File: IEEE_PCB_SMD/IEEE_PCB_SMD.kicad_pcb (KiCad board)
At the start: 2 copper layers, 98.9 x 105.3 mm, 18 parts, among them U1 555, U2 4017, U3 EG1218, U4 1058TR

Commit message: SMD Rev3
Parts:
- added D10: D, IEEE_PCB_Ornament:SDM20U40Q, F.Cu at (153.6, 81.5)
- added D11: D, IEEE_PCB_Ornament:SDM20U40Q, F.Cu at (153.6, 84.2)
- added D12: D, IEEE_PCB_Ornament:SDM20U40Q, F.Cu at (153.6, 86.9)
- added G***: LOGO, Logos:IEEE Logo, F.Cu at (141.4, 100.6)
- added U5: CR2025TR, IEEE_PCB_Ornament:CR2025TR, F.Cu at (145.0, 95.8)
- RV1: value 500K -> 100K
- U4: value 1058TR -> EG1218; footprint IEEE_PCB_Ornament:1058TR -> IEEE_PCB_Ornament:EG1218
- moved D3 68.2 mm to (145.7, 128.7)
- moved D2 59.8 mm to (177.0, 74.9), turned to 90 degrees
- moved U4 20.3 mm to (152.2, 111.8), turned to 0 degrees
- moved RV1 19.5 mm to (145.0, 80.7)
- moved U3 13.1 mm to (138.5, 111.8)
- moved D8 10.9 mm to (144.9, 88.7), turned to 180 degrees
- moved C2 10.4 mm to (131.4, 93.4)
- moved D9 9.58 mm to (148.7, 94.5), turned to 0 degrees
- moved U2 9.21 mm to (157.3, 79.3)
- moved C1 8.84 mm to (125.0, 93.1)
- moved D7 7.04 mm to (141.2, 94.5)
- moved D6 6.50 mm to (176.2, 112.6), turned to 90 degrees
- moved D1 6.48 mm to (114.4, 74.7), turned to 270 degrees
- moved R1 6.45 mm to (138.7, 73.9)
- moved D4 6.29 mm to (144.8, 57.4)
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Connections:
- D1 pad 2: Net-(D1-Pad2) -> ALLON
- D2 pad 2: Net-(D1-Pad2) -> ALLON
- D3 pad 2: Net-(D1-Pad2) -> ALLON
- D4 pad 2: Net-(D4-Pad2) -> ALLON
- D5 pad 2: Net-(D4-Pad2) -> ALLON
- D6 pad 2: Net-(D4-Pad2) -> ALLON
- D7 pad 2: Net-(D7-Pad2) -> ALLON
- D8 pad 2: Net-(D7-Pad2) -> ALLON
- D9 pad 2: Net-(D7-Pad2) -> ALLON
- U2 pad 2: Net-(D1-Pad2) -> Net-(D10-Pad2)
- U2 pad 3: Net-(D4-Pad2) -> Net-(D11-Pad2)
- U2 pad 4: Net-(D7-Pad2) -> Net-(D12-Pad2)
- U3 pad 1: +3V3 -> Net-(U3-Pad1)
- U3 pad 3: GND -> Net-(U3-Pad3)
- U4 pad 1: Net-(U3-Pad2) -> +3V3
- U4 pad 2: GND -> Net-(U3-Pad1)
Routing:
- net ALLON: track 0.00 -> 283.9 mm, vias 0 -> 10
- net GND: track 6.63 -> 148.7 mm, vias 0 -> 13
- net Net-(D4-Pad2): track 130.3 -> 0.00 mm, vias 3 -> 0
- net Net-(D1-Pad2): track 129.5 -> 0.00 mm, vias 2 -> 0
- net Net-(D7-Pad2): track 20.2 -> 0.00 mm
- net Net-(U3-Pad1): track 0.00 -> 17.6 mm
- net Net-(R1-Pad2): track 38.1 -> 23.7 mm
- net Net-(C2-Pad1): track 51.3 -> 44.7 mm
- net Net-(D10-Pad2): track 0.00 -> 3.14 mm
- net Net-(D11-Pad2): track 0.00 -> 3.07 mm
- net Net-(D12-Pad2): track 0.00 -> 3.01 mm
- net +3V3: track 100.1 -> 102.7 mm
- net Net-(U2-Pad15): track 17.8 -> 15.9 mm
- net Net-(U3-Pad2): track 41.2 -> 43.2 mm, vias 2 -> 0
- net Net-(C1-Pad1): track 13.6 -> 12.4 mm
- added copper zone on B.Cu, net ALLON
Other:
- board size 98.9 x 105.3 mm -> 98.9 x 105.4 mm
- board text added: "REV1"
- board text added: "UCSB IEEE"

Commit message: Rev4 SMD
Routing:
- net ALLON: track 283.9 -> 473.5 mm, vias 10 -> 14
- net GND: track 148.7 -> 157.5 mm
- removed copper zone on B.Cu, net ALLON

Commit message: Rev5 SMD
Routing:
- net +3V3: track 102.7 -> 86.3 mm, vias 0 -> 1
- net ALLON: track 473.5 -> 472.8 mm

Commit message: Rev4
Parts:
- removed D10, D11, D12: D, IEEE_PCB_Ornament:SDM20U40Q
- removed the G*** at (141.4, 100.6)
- removed U4: EG1218, IEEE_PCB_Ornament:EG1218
- added G***: LOGO, custom parts:IEEE Logo, F.Cu at (143.9, 103.0)
- D1, D2, D3, D4, D5, D6, D7, D8, D9: footprint IEEE_PCB_Ornament:LED_SMD -> IEEE_Ornament:IN-S63AT
- RV1: value 100K -> 50K; footprint IEEE_PCB_Ornament:CT6EP504 -> IEEE_Ornament:CT6EP504
- U1: footprint IEEE_PCB_Ornament:555 -> IEEE_Ornament:555
- U2: footprint IEEE_PCB_Ornament:4017 -> IEEE_Ornament:4017
- U3: footprint IEEE_PCB_Ornament:EG1218 -> IEEE_Ornament:EG1218
- U5: footprint IEEE_PCB_Ornament:CR2025TR -> IEEE_Ornament:CR2025TR
- moved D5 73.8 mm to (180.0, 75.2), turned to 180 degrees
- moved D2 68.2 mm to (118.2, 109.6), turned to 0 degrees
- moved D1 38.0 mm to (148.0, 57.0)
- moved D3 36.8 mm to (178.0, 111.1), turned to 180 degrees
- moved D6 32.2 mm to (148.6, 129.2)
- moved D4 31.9 mm to (117.7, 74.2), turned to 0 degrees
- moved U3 9.55 mm to (148.1, 111.7)
- moved D7 7.95 mm to (148.0, 90.4), turned to -90 degrees
- moved D8 7.55 mm to (144.4, 96.2), turned to 90 degrees
- moved D9 3.50 mm to (151.8, 96.1), turned to 90 degrees
- moved C2 3.42 mm to (134.8, 93.9)
- moved U5 3.18 mm to (148.2, 95.8)
- moved REF** 3.14 mm to (100.5, 99.0)
- moved U1 2.96 mm to (130.3, 79.7)
- moved U2 2.93 mm to (160.1, 80.2)
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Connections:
- D1 pad 2: ALLON -> Net-(D1-Pad2)
- D2 pad 2: ALLON -> Net-(D1-Pad2)
- D3 pad 2: ALLON -> Net-(D1-Pad2)
- D4 pad 2: ALLON -> Net-(D4-Pad2)
- D5 pad 2: ALLON -> Net-(D4-Pad2)
- D6 pad 2: ALLON -> Net-(D4-Pad2)
- D7 pad 2: ALLON -> Net-(D7-Pad2)
- D8 pad 2: ALLON -> Net-(D7-Pad2)
- D9 pad 2: ALLON -> Net-(D7-Pad2)
- U2 pad 1: Net-(U2-Pad1) -> unconnected-(U2-Pad1)
- U2 pad 10: Net-(U2-Pad10) -> unconnected-(U2-Pad10)
- U2 pad 11: Net-(U2-Pad11) -> unconnected-(U2-Pad11)
- U2 pad 12: Net-(U2-Pad12) -> unconnected-(U2-Pad12)
- U2 pad 2: Net-(D10-Pad2) -> Net-(D1-Pad2)
- U2 pad 3: Net-(D11-Pad2) -> Net-(D4-Pad2)
- U2 pad 4: Net-(D12-Pad2) -> Net-(D7-Pad2)
- U2 pad 5: Net-(U2-Pad5) -> unconnected-(U2-Pad5)
- U2 pad 6: Net-(U2-Pad6) -> unconnected-(U2-Pad6)
- U2 pad 9: Net-(U2-Pad9) -> unconnected-(U2-Pad9)
- U3 pad 1: Net-(U3-Pad1) -> +3V3
- U3 pad 3: Net-(U3-Pad3) -> unconnected-(U3-Pad3)
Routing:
- net ALLON: track 472.8 -> 0.00 mm, vias 14 -> 0
- net GND: track 157.5 -> 0.00 mm, vias 13 -> 21
- net Net-(D4-Pad2): track 0.00 -> 125.6 mm, vias 0 -> 4
- net Net-(D1-Pad2): track 0.00 -> 118.8 mm, vias 0 -> 1
- net Net-(D7-Pad2): track 0.00 -> 24.7 mm
- net Net-(U3-Pad1): track 17.6 -> 0.00 mm
- net +3V3: track 86.3 -> 102.4 mm, vias 1 -> 0
- net Net-(C2-Pad1): track 44.7 -> 31.5 mm
- net Net-(U2-Pad15): track 15.9 -> 22.4 mm, vias 0 -> 2
- net Net-(D10-Pad2): track 3.14 -> 0.00 mm
- net Net-(D11-Pad2): track 3.07 -> 0.00 mm
- net Net-(D12-Pad2): track 3.01 -> 0.00 mm
- net Net-(U3-Pad2): track 43.2 -> 41.7 mm
- net Net-(C1-Pad1): track 12.4 -> 13.7 mm
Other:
- board size 98.9 x 105.4 mm -> 98.9 x 105.3 mm
- net class Default removed

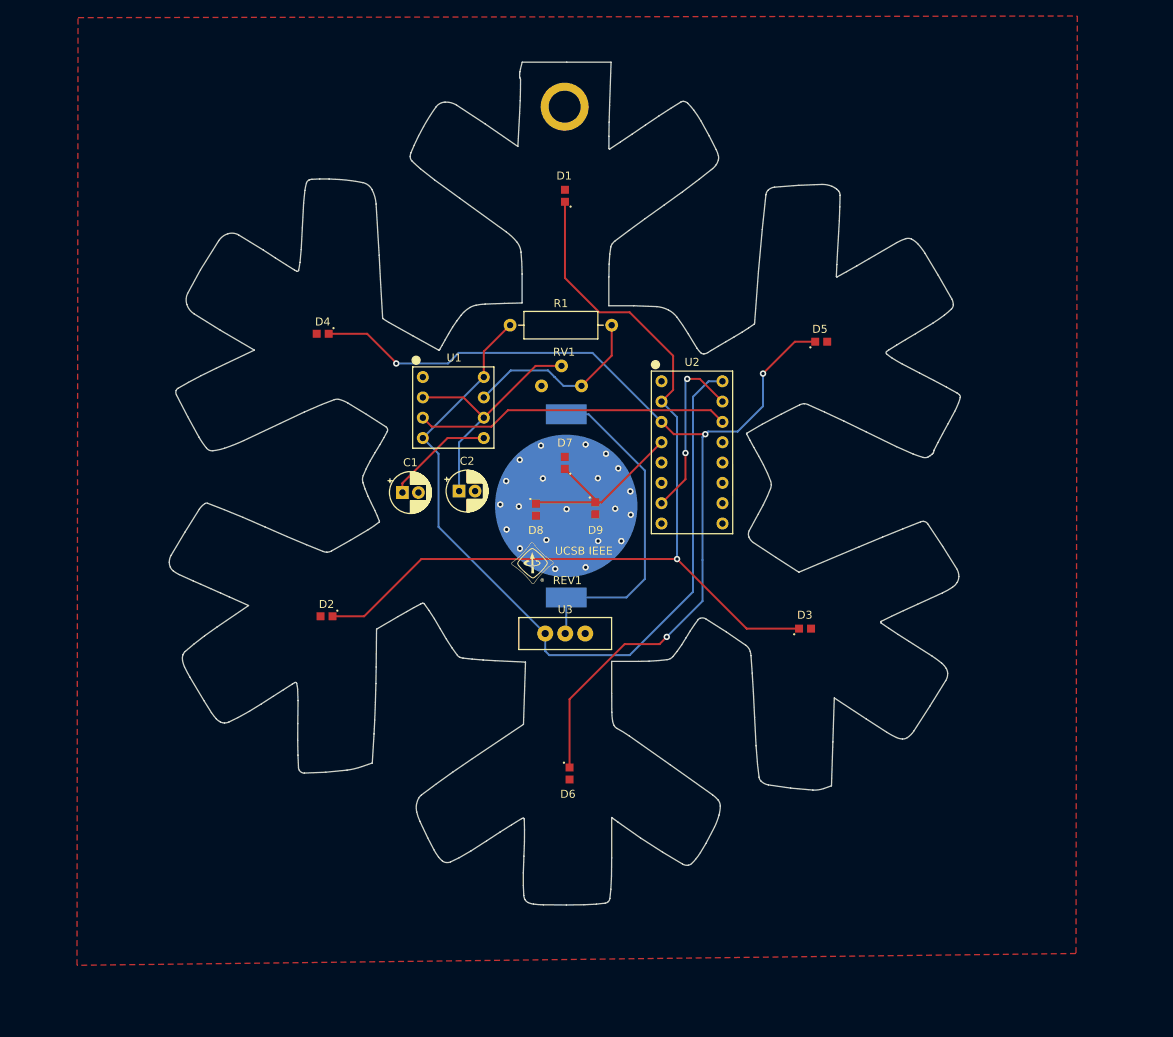
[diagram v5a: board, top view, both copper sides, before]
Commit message: changed trace
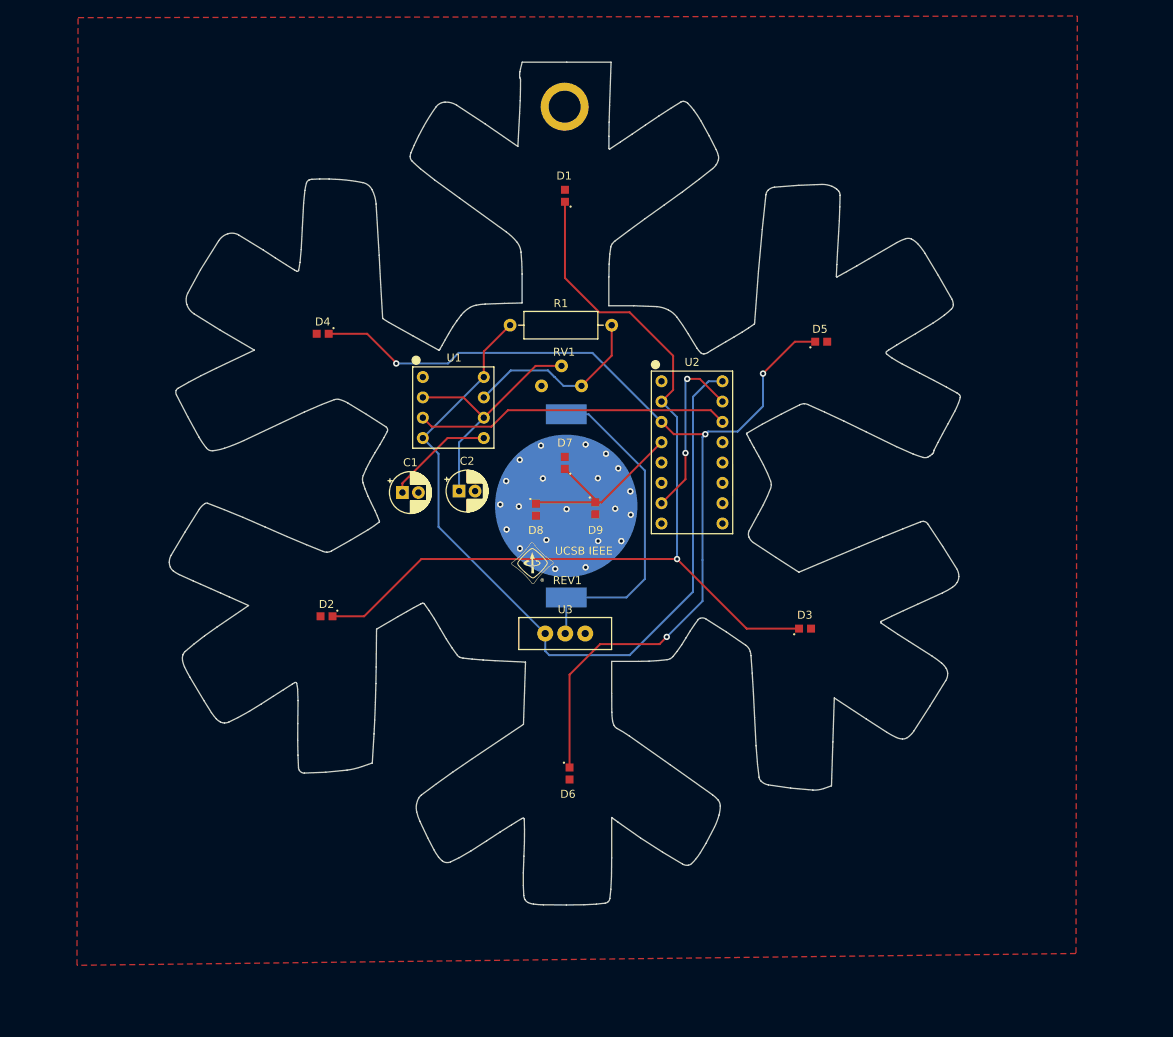
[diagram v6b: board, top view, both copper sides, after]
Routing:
- net Net-(D4-Pad2): track 125.6 -> 127.4 mm
